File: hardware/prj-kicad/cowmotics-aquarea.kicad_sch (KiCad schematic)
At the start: 0 parts

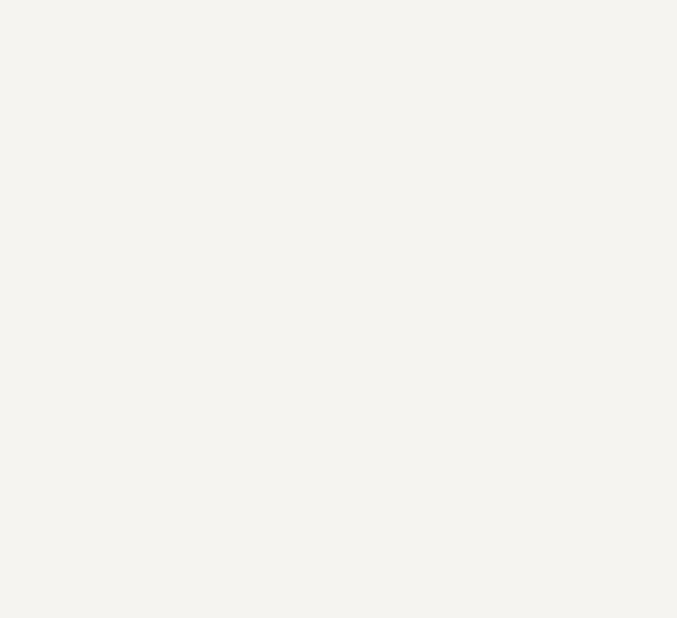
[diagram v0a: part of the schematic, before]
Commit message: = ADD: Insert ESP32 processor and his main components
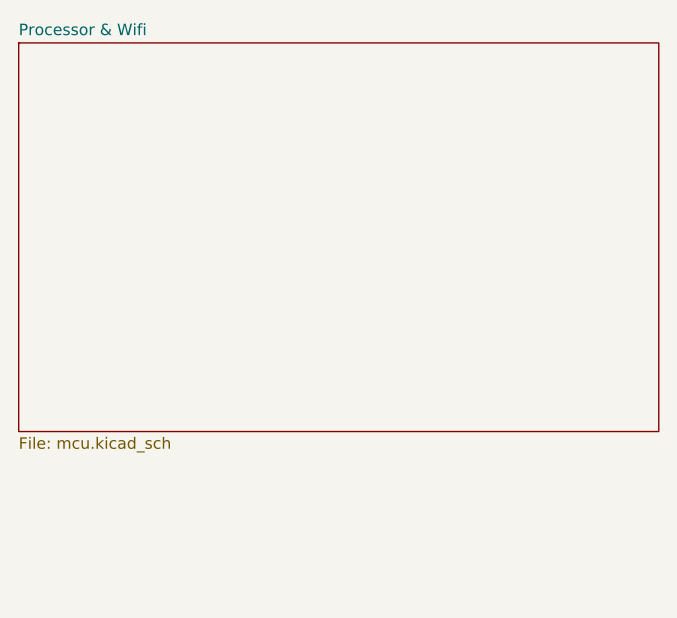
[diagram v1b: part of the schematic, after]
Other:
- added sheet Processor & Wifi (mcu.kicad_sch)
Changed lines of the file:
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@@
+    )
+  )
+  (sheet (at 135.89 33.655) (size 71.12 43.18) (fields_autoplaced)
+    (stroke (width 0.1524) (type solid) (color 0 0 0 0))
+    (fill (color 0 0 0 0.0000))
+    (property "Sheet name" "Processor & Wifi" (id 0) (at 135.89 32.9434 0)
+      (effects (font (size 1.27 1.27)) (justify left bottom))
+    )
+    (property "Sheet file" "mcu.kicad_sch" (id 1) (at 135.89 77.4196 0)
+      (effects (font (size 1.27 1.27)) (justify left top))
     )
   )
@@
     (path "/" (page "1"))
     (path "/38d2e88e-817b-499b-a8dc-6ffe82e53baa" (page "2"))
+    (path "/825065db-dc11-43e9-aa2e-59e6b2cd21f3" (page "3"))
   )
   (symbol_instances
@@
       (reference "#PWR0125") (unit 1) (value "GND") (footprint "")
     )
+    (path "/825065db-dc11-43e9-aa2e-59e6b2cd21f3/aa662617-353d-45f8-8bab-007a7f6b3467"
+      (reference "#PWR0126") (unit 1) (value "GND") (footprint "")
+    )
+    (path "/825065db-dc11-43e9-aa2e-59e6b2cd21f3/f5a690b1-a723-491f-9e65-a4dc1fb25333"
+      (reference "#PWR0127") (unit 1) (value "GND") (footprint "")
+    )
+    (path "/825065db-dc11-43e9-aa2e-59e6b2cd21f3/bb7c498b-0339-4089-b873-6dffa6d6713f"
+      (reference "#PWR0128") (unit 1) (value "GND") (footprint "")
+    )
+    (path "/825065db-dc11-43e9-aa2e-59e6b2cd21f3/367afd26-be8b-422a-ab8f-fbd169ddcc5a"
+      (reference "#PWR0129") (unit 1) (value "GND") (footprint "")
+    )
+    (path "/825065db-dc11-43e9-aa2e-59e6b2cd21f3/98364297-c4ad-454c-b800-3e22ff1db8a3"
+      (reference "#PWR0130") (unit 1) (value "GND") (footprint "")
+    )
+    (path "/825065db-dc11-43e9-aa2e-59e6b2cd21f3/55887181-5e4b-4575-b90e-fe6bb9328e01"
+      (reference "#PWR0131") (unit 1) (value "GND") (footprint "")
+    )
+    (path "/825065db-dc11-43e9-aa2e-59e6b2cd21f3/9cf5069d-7e57-418e-8c23-95dcafcdacf9"
+      (reference "#PWR0132") (unit 1) (value "+3.3V") (footprint "")
+    )
+    (path "/825065db-dc11-43e9-aa2e-59e6b2cd21f3/33c6b2c3-1517-422e-85ee-b8426af14ec5"
+      (reference "#PWR0133") (unit 1) (value "+3.3V") (footprint "")
+    )
+    (path "/825065db-dc11-43e9-aa2e-59e6b2cd21f3/abdb3229-d2e1-49d3-b8de-37b672350f4f"
+      (reference "#PWR0134") (unit 1) (value "+3.3V") (footprint "")
+    )
+    (path "/825065db-dc11-43e9-aa2e-59e6b2cd21f3/a6f2707f-c9c9-4cbb-9ba7-d37e52c8a8a4"
+      (reference "#PWR0135") (unit 1) (value "GND") (footprint "")
+    )
+    (path "/825065db-dc11-43e9-aa2e-59e6b2cd21f3/3ec4ff8a-4c7d-42d9-a1a2-4060e56d921d"
+      (reference "#PWR0136") (unit 1) (value "GND") (footprint "")
+    )
+    (path "/825065db-dc11-43e9-aa2e-59e6b2cd21f3/5bc6b76e-0764-45bf-b282-a3a5393cd86d"
+      (reference "#PWR0137") (unit 1) (value "GND") (footprint "")
+    )
+    (path "/825065db-dc11-43e9-aa2e-59e6b2cd21f3/ac896b10-b56d-48cd-a40f-40aea60ea3de"
+      (reference "#PWR0138") (unit 1) (value "GND") (footprint "")
+    )
+    (path "/825065db-dc11-43e9-aa2e-59e6b2cd21f3/f72bf72c-f5bd-4416-9db8-2d2131c42563"
+      (reference "#PWR0139") (unit 1) (value "+3.3V") (footprint "")
+    )
+    (path "/825065db-dc11-43e9-aa2e-59e6b2cd21f3/2d06930a-3556-4ca4-8e19-ceb5186c902c"
+      (reference "#PWR0140") (unit 1) (value "GND") (footprint "")
+    )
+    (path "/825065db-dc11-43e9-aa2e-59e6b2cd21f3/c1353406-aee2-4fa7-afd8-e1c3846e03ff"
+      (reference "#PWR0141") (unit 1) (value "GND") (footprint "")
+    )
+    (path "/825065db-dc11-43e9-aa2e-59e6b2cd21f3/1a96750d-1856-4066-bb83-1223e7a4075b"
+      (reference "#PWR0142") (unit 1) (value "GND") (footprint "")
+    )
+    (path "/825065db-dc11-43e9-aa2e-59e6b2cd21f3/59a86aaa-3c97-4075-abdb-4a0f75c3444c"
+      (reference "#PWR0143") (unit 1) (value "+VMEM") (footprint "")
+    )
+    (path "/825065db-dc11-43e9-aa2e-59e6b2cd21f3/70b0bb82-e5bb-4e37-8438-bc5be16178cc"
+      (reference "#PWR0144") (unit 1) (value "+VMEM") (footprint "")
+    )
+    (path "/825065db-dc11-43e9-aa2e-59e6b2cd21f3/ab3fca1c-45bb-469f-9f25-aa7e33ef6c3f"
+      (reference "#PWR0145") (unit 1) (value "+VMEM") (footprint "")
+    )
+    (path "/825065db-dc11-43e9-aa2e-59e6b2cd21f3/faf896ff-a31a-44d8-9988-76831a9d862a"
+      (reference "#PWR0146") (unit 1) (value "GND") (footprint "")
+    )
+    (path "/825065db-dc11-43e9-aa2e-59e6b2cd21f3/e7cc7ad7-f806-48cf-ae6e-20dfcc5dcaee"
+      (reference "A1") (unit 1) (value "ANTENNA") (footprint "")
+    )
     (path "/38d2e88e-817b-499b-a8dc-6ffe82e53baa/e4901cdd-b675-43fa-95c2-426e8c824f2f"
       (reference "C1") (unit 1) (value "100nF") (footprint "cowmotics-aquarea:SMD0603")
@@
       (reference "C9") (unit 1) (value "100nF") (footprint "cowmotics-aquarea:SMD0603")
     )
+    (path "/825065db-dc11-43e9-aa2e-59e6b2cd21f3/b412f3cc-d747-49e4-af3e-b05be88e1086"
+      (reference "C11") (unit 1) (value "10pF") (footprint "cowmotics-aquarea:SMD0603")
+    )
+    (path "/825065db-dc11-43e9-aa2e-59e6b2cd21f3/27b131df-df48-47ca-b698-fc59bb8b7b48"
+      (reference "C12") (unit 1) (value "10pF") (footprint "cowmotics-aquarea:SMD0603")
+    )
+    (path "/825065db-dc11-43e9-aa2e-59e6b2cd21f3/dc627a33-8631-4bf7-9cfa-e7d61c1c50ec"
+      (reference "C13") (unit 1) (value "10nF") (footprint "cowmotics-aquarea:SMD0603")
+    )
+    (path "/825065db-dc11-43e9-aa2e-59e6b2cd21f3/055bd41d-4d87-4a49-9e0d-ec28a81d5e69"
+      (reference "C14") (unit 1) (value "10nF") (footprint "cowmotics-aquarea:SMD0603")
+    )
+    (path "/825065db-dc11-43e9-aa2e-59e6b2cd21f3/1da82e5d-dfed-41b2-ba5e-3a1d68571e18"
+      (reference "C15") (unit 1) (value "3,3nF") (footprint "cowmotics-aquarea:SMD0603")
+    )
+    (path "/825065db-dc11-43e9-aa2e-59e6b2cd21f3/2e5dae1f-76cb-4c37-85a0-30b2c21af63f"
+      (reference "C16") (unit 1) (value "C") (footprint "cowmotics-aquarea:SMD0603")
+    )
+    (path "/825065db-dc11-43e9-aa2e-59e6b2cd21f3/cc4d6061-2845-4d3f-a4f9-82eeb84d6d9f"
+      (reference "C17") (unit 1) (value "C") (footprint "cowmotics-aquarea:SMD0603")
+    )
+    (path "/825065db-dc11-43e9-aa2e-59e6b2cd21f3/aaea601f-301e-4b17-bbc4-978a8026e72b"
+      (reference "C18") (unit 1) (value "1uF") (footprint "cowmotics-aquarea:SMD0603")
+    )
+    (path "/825065db-dc11-43e9-aa2e-59e6b2cd21f3/8ec30f0d-54f3-4133-ad28-83d66580ed3b"
+      (reference "C19") (unit 1) (value "100nF") (footprint "cowmotics-aquarea:SMD0603")
+    )
+    (path "/825065db-dc11-43e9-aa2e-59e6b2cd21f3/9d2bfb75-3655-468a-99b3-1689c86cc127"
+      (reference "C20") (unit 1) (value "100nF") (footprint "cowmotics-aquarea:SMD0603")
+    )
     (path "/38d2e88e-817b-499b-a8dc-6ffe82e53baa/18a9dea8-caa6-40a3-962a-7699d9146e17"
       (reference "J1") (unit 1) (value "CONN_RJ45") (footprint "cowmotics-aquarea:CONN_615008185121")
@@
       (reference "L1") (unit 1) (value "FB100") (footprint "cowmotics-aquarea:SMD0603")
     )
+    (path "/825065db-dc11-43e9-aa2e-59e6b2cd21f3/36f39277-833d-4032-80bf-37be5c675044"
+      (reference "L2") (unit 1) (value "FB100") (footprint "cowmotics-aquarea:SMD0603")
+    )
+    (path "/825065db-dc11-43e9-aa2e-59e6b2cd21f3/0d087c84-db65-4f93-8a04-a5da574852b7"
+      (reference "L3") (unit 1) (value "INDUCTOR") (footprint "cowmotics-aquarea:SMD0603")
+    )
     (path "/38d2e88e-817b-499b-a8dc-6ffe82e53baa/bea8a93b-5d86-4516-aa08-d642cf48f2e6"
       (reference "Q1") (unit 1) (value "BC846") (footprint "cowmotics-aquarea:SOT23-3")
@@
       (reference "R12") (unit 1) (value "10k") (footprint "cowmotics-aquarea:SMD0603")
     )
+    (path "/825065db-dc11-43e9-aa2e-59e6b2cd21f3/0df40f43-d59d-4bf1-b2e8-22aead9235c5"
+      (reference "R15") (unit 1) (value "10k") (footprint "cowmotics-aquarea:SMD0603")
+    )
+    (path "/825065db-dc11-43e9-aa2e-59e6b2cd21f3/ac2da823-4699-45dd-9813-e8de59e5d43b"
+      (reference "R16") (unit 1) (value "20k") (footprint "cowmotics-aquarea:SMD0603")
+    )
     (path "/38d2e88e-817b-499b-a8dc-6ffe82e53baa/a56deef6-ff70-4f97-bfaa-cc479299031a"
       (reference "T1") (unit 1) (value "TRANSFORMER_1_1") (footprint "cowmotics-aquarea:TR_W749013011")
@@
       (reference "U1") (unit 1) (value "KSZ8091RN") (footprint "cowmotics-aquarea:QFN24")
     )
+    (path "/825065db-dc11-43e9-aa2e-59e6b2cd21f3/53eb5fc0-41cc-43ad-8003-3a7163adca82"
+      (reference "U2") (unit 1) (value "ESP32") (footprint "cowmotics-aquarea:QFN48-04")
+    )
+    (path "/825065db-dc11-43e9-aa2e-59e6b2cd21f3/6ead67cb-c858-432f-8293-babe98d42987"
+      (reference "U2") (unit 2) (value "ESP32") (footprint "cowmotics-aquarea:QFN48-04")
+    )
+    (path "/825065db-dc11-43e9-aa2e-59e6b2cd21f3/f5db3b34-82eb-4087-85c1-08c4586de2aa"
+      (reference "U3") (unit 1) (value "SST25VF016") (footprint "cowmotics-aquarea:SOIC-8")
+    )
     (path "/38d2e88e-817b-499b-a8dc-6ffe82e53baa/bdfc4715-c6ee-47ec-8978-077838963a54"
       (reference "X1") (unit 1) (value "50MHz") (footprint "cowmotics-aquarea:Q_SMD5x3")
     )
-  )
+    (path "/825065db-dc11-43e9-aa2e-59e6b2cd21f3/bdbb5037-e302-4f21-aecd-679af5c21a62"
+      (reference "X2") (unit 1) (value "40MHz") (footprint "cowmotics-aquarea:Q_3.2x2.5")
+    )
+  )

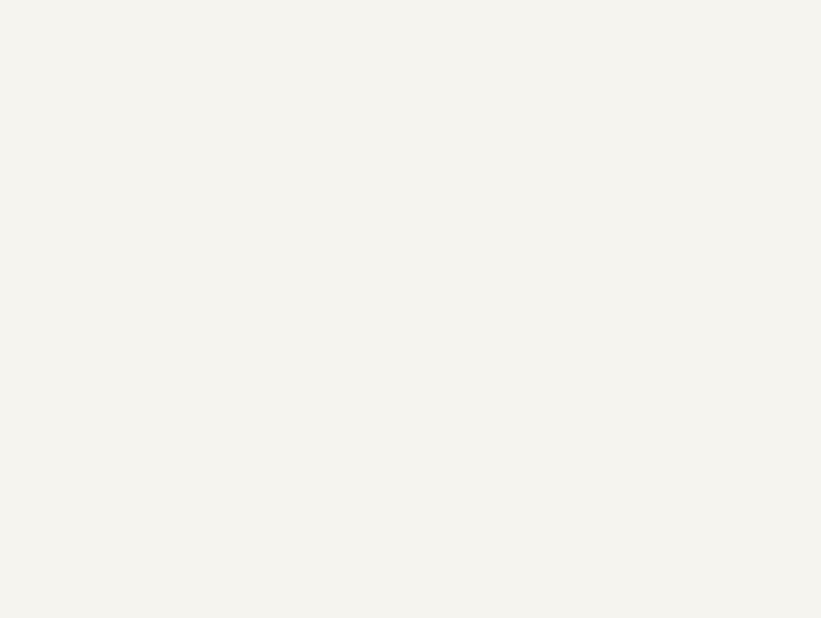
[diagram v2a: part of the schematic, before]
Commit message: = ADD: Insert Aquarea serial interface and power supply
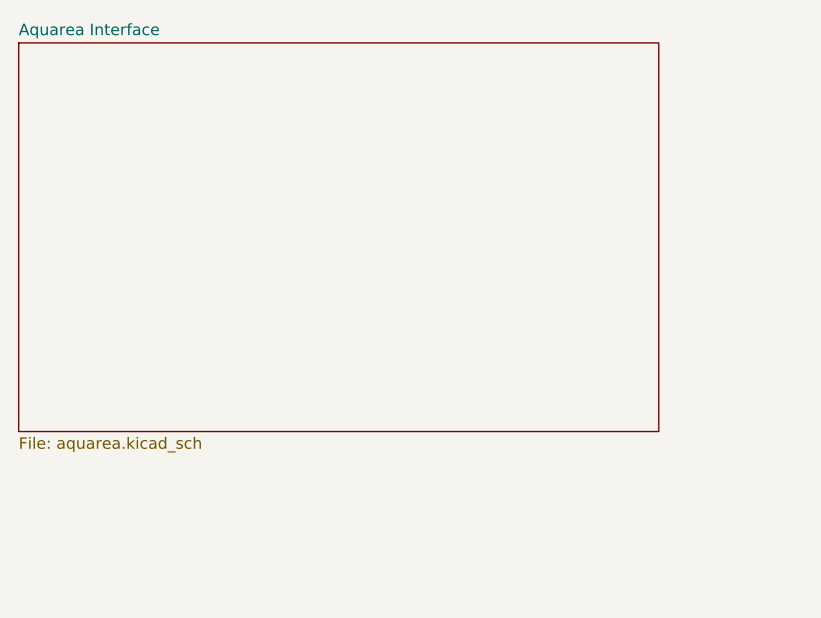
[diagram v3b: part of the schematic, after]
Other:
- added sheet Aquarea Interface (aquarea.kicad_sch)
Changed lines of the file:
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@@
+    )
+  )
+  (sheet (at 33.655 33.655) (size 71.12 43.18) (fields_autoplaced)
+    (stroke (width 0.1524) (type solid) (color 0 0 0 0))
+    (fill (color 0 0 0 0.0000))
+    (property "Sheet name" "Aquarea Interface" (id 0) (at 33.655 32.9434 0)
+      (effects (font (size 1.27 1.27)) (justify left bottom))
+    )
+    (property "Sheet file" "aquarea.kicad_sch" (id 1) (at 33.655 77.4196 0)
+      (effects (font (size 1.27 1.27)) (justify left top))
     )
   )
@@
     (path "/38d2e88e-817b-499b-a8dc-6ffe82e53baa" (page "2"))
     (path "/825065db-dc11-43e9-aa2e-59e6b2cd21f3" (page "3"))
+    (path "/98155800-78e7-48e2-b416-a5948d22b132" (page "4"))
   )
   (symbol_instances
@@
       (reference "#PWR0154") (unit 1) (value "GND") (footprint "")
     )
+    (path "/98155800-78e7-48e2-b416-a5948d22b132/a24579c0-8f16-4c68-b896-1ec34d92a6c4"
+      (reference "#PWR0155") (unit 1) (value "+5V") (footprint "")
+    )
+    (path "/98155800-78e7-48e2-b416-a5948d22b132/df4a707f-c422-45b9-846e-5f8beda1b995"
+      (reference "#PWR0156") (unit 1) (value "GND") (footprint "")
+    )
+    (path "/98155800-78e7-48e2-b416-a5948d22b132/8941ba23-15e2-4939-ba0d-2ca7f1f5ac1b"
+      (reference "#PWR0157") (unit 1) (value "+3.3V") (footprint "")
+    )
+    (path "/98155800-78e7-48e2-b416-a5948d22b132/f8b6bb9f-ad03-4bcb-9251-2a066978a098"
+      (reference "#PWR0158") (unit 1) (value "+5V") (footprint "")
+    )
+    (path "/98155800-78e7-48e2-b416-a5948d22b132/deb3c8d4-cd4a-4c3f-9749-bd9ef6b7b0d7"
+      (reference "#PWR0159") (unit 1) (value "GND") (footprint "")
+    )
+    (path "/98155800-78e7-48e2-b416-a5948d22b132/2523fb7d-bdf6-476e-87d5-a6e44e66f2d6"
+      (reference "#PWR0160") (unit 1) (value "+12V") (footprint "")
+    )
+    (path "/98155800-78e7-48e2-b416-a5948d22b132/ae02e6ad-b22a-4981-9b68-ea9b5483cbf0"
+      (reference "#PWR0161") (unit 1) (value "+5V") (footprint "")
+    )
+    (path "/98155800-78e7-48e2-b416-a5948d22b132/cc9ecc58-049e-4be1-b641-c31882f37ca7"
+      (reference "#PWR0162") (unit 1) (value "+3.3V") (footprint "")
+    )
+    (path "/98155800-78e7-48e2-b416-a5948d22b132/4e51c7be-5689-4060-9944-a768ee0964e6"
+      (reference "#PWR0163") (unit 1) (value "GND") (footprint "")
+    )
+    (path "/98155800-78e7-48e2-b416-a5948d22b132/76d96292-67d7-4661-baf1-dfdd20b23b48"
+      (reference "#PWR0164") (unit 1) (value "GND") (footprint "")
+    )
+    (path "/98155800-78e7-48e2-b416-a5948d22b132/8c35d187-d2af-4c4c-a5db-5041491ae221"
+      (reference "#PWR0165") (unit 1) (value "+3.3V") (footprint "")
+    )
+    (path "/98155800-78e7-48e2-b416-a5948d22b132/960e3980-6992-4f2f-be18-9d55b25deb4f"
+      (reference "#PWR0166") (unit 1) (value "+5V") (footprint "")
+    )
+    (path "/98155800-78e7-48e2-b416-a5948d22b132/646eb608-8655-4892-b3d9-d0c69b132ad5"
+      (reference "#PWR0167") (unit 1) (value "GND") (footprint "")
+    )
+    (path "/98155800-78e7-48e2-b416-a5948d22b132/dd76ffd3-cf84-4264-9b48-46e38b2e06ed"
+      (reference "#PWR0168") (unit 1) (value "GND") (footprint "")
+    )
+    (path "/98155800-78e7-48e2-b416-a5948d22b132/070569f3-8118-41a9-ae0d-9ac889645e9d"
+      (reference "#PWR0169") (unit 1) (value "GND") (footprint "")
+    )
+    (path "/98155800-78e7-48e2-b416-a5948d22b132/105c56d1-30e6-4a56-976f-42759cb1f7f2"
+      (reference "#PWR0170") (unit 1) (value "+3.3V") (footprint "")
+    )
+    (path "/98155800-78e7-48e2-b416-a5948d22b132/8152e6f5-b60f-4c0c-ac89-7de02362ab60"
+      (reference "#PWR0171") (unit 1) (value "GND") (footprint "")
+    )
+    (path "/98155800-78e7-48e2-b416-a5948d22b132/05b16ca9-6086-4d32-aa87-2738c8656874"
+      (reference "#PWR0172") (unit 1) (value "+12V") (footprint "")
+    )
+    (path "/98155800-78e7-48e2-b416-a5948d22b132/6da368c0-01b4-4b20-8f83-3377f60df388"
+      (reference "#PWR0173") (unit 1) (value "GND") (footprint "")
+    )
+    (path "/98155800-78e7-48e2-b416-a5948d22b132/1302e146-4d18-4a35-b511-025dc46a5910"
+      (reference "#PWR0174") (unit 1) (value "+5V") (footprint "")
+    )
+    (path "/98155800-78e7-48e2-b416-a5948d22b132/110987fe-4f33-4568-96f4-a15ba51a26fb"
+      (reference "#PWR0175") (unit 1) (value "GND") (footprint "")
+    )
+    (path "/98155800-78e7-48e2-b416-a5948d22b132/12fa97ca-9c7c-4df1-bac7-aa03d210c139"
+      (reference "#PWR0176") (unit 1) (value "GND") (footprint "")
+    )
+    (path "/98155800-78e7-48e2-b416-a5948d22b132/035aefe0-7417-4380-8cad-ff04e2942bb6"
+      (reference "#PWR0177") (unit 1) (value "GND") (footprint "")
+    )
+    (path "/98155800-78e7-48e2-b416-a5948d22b132/2397e841-1be1-415f-a1b9-7ff8d54aff04"
+      (reference "#PWR0178") (unit 1) (value "+3.3V") (footprint "")
+    )
     (path "/825065db-dc11-43e9-aa2e-59e6b2cd21f3/e7cc7ad7-f806-48cf-ae6e-20dfcc5dcaee"
       (reference "A1") (unit 1) (value "ANTENNA") (footprint "cowmotics-aquarea:CONN_SMA_RA")
@@
       (reference "C23") (unit 1) (value "1uF") (footprint "cowmotics-aquarea:SMD0603")
     )
+    (path "/98155800-78e7-48e2-b416-a5948d22b132/53279ea3-2f0b-40ec-b25e-0a09cafac841"
+      (reference "C25") (unit 1) (value "10uF") (footprint "cowmotics-aquarea:SMD1210")
+    )
+    (path "/98155800-78e7-48e2-b416-a5948d22b132/113db992-658b-4f23-8b16-4522e5d594a2"
+      (reference "C26") (unit 1) (value "100nF") (footprint "cowmotics-aquarea:SMD0603")
+    )
+    (path "/98155800-78e7-48e2-b416-a5948d22b132/8d3a9eec-e9a7-4f7a-a913-1c4b83c46ec3"
+      (reference "C27") (unit 1) (value "100nF") (footprint "cowmotics-aquarea:SMD0603")
+    )
+    (path "/98155800-78e7-48e2-b416-a5948d22b132/7844fa1c-c2e9-46d4-aee9-55128915096f"
+      (reference "C28") (unit 1) (value "10uF") (footprint "cowmotics-aquarea:SMD1210")
+    )
+    (path "/98155800-78e7-48e2-b416-a5948d22b132/e82ebb99-a6b9-48fa-9aa1-331985f42c93"
+      (reference "C29") (unit 1) (value "470pF") (footprint "cowmotics-aquarea:SMD0603")
+    )
+    (path "/98155800-78e7-48e2-b416-a5948d22b132/b3b5d4a8-a7a4-4bdd-91c8-1d396734d302"
+      (reference "C30") (unit 1) (value "4,7uF") (footprint "cowmotics-aquarea:SMD0603")
+    )
+    (path "/98155800-78e7-48e2-b416-a5948d22b132/feda6d61-2233-4f26-b0c5-c1eee19352ad"
+      (reference "C31") (unit 1) (value "4,7uF") (footprint "cowmotics-aquarea:SMD0603")
+    )
     (path "/38d2e88e-817b-499b-a8dc-6ffe82e53baa/18a9dea8-caa6-40a3-962a-7699d9146e17"
       (reference "J1") (unit 1) (value "CONN_RJ45") (footprint "cowmotics-aquarea:CONN_615008185121")
     )
+    (path "/98155800-78e7-48e2-b416-a5948d22b132/91125ed1-04ac-414b-89bd-9ef46367e239"
+      (reference "J2") (unit 1) (value "CONN_5") (footprint "cowmotics-aquarea:CONN_691243310005")
+    )
     (path "/38d2e88e-817b-499b-a8dc-6ffe82e53baa/ec075aee-9a67-4dd0-9403-ff58215d0638"
       (reference "L1") (unit 1) (value "FB100") (footprint "cowmotics-aquarea:SMD0603")
@@
       (reference "L3") (unit 1) (value "INDUCTOR") (footprint "cowmotics-aquarea:SMD0603")
     )
+    (path "/98155800-78e7-48e2-b416-a5948d22b132/84c6da4f-5623-4a9c-a50d-ae757f720ada"
+      (reference "L4") (unit 1) (value "2,2uH") (footprint "cowmotics-aquarea:I_CDRH2D14")
+    )
     (path "/38d2e88e-817b-499b-a8dc-6ffe82e53baa/bea8a93b-5d86-4516-aa08-d642cf48f2e6"
       (reference "Q1") (unit 1) (value "BC846") (footprint "cowmotics-aquarea:SOT23-3")
@@
       (reference "U3") (unit 1) (value "SST25VF016") (footprint "cowmotics-aquarea:SOIC-8")
     )
+    (path "/98155800-78e7-48e2-b416-a5948d22b132/5460fda9-d078-489b-9094-c02aef678b0d"
+      (reference "U4") (unit 1) (value "SN74LVC1T45") (footprint "cowmotics-aquarea:SOT23-6")
+    )
+    (path "/98155800-78e7-48e2-b416-a5948d22b132/2d49add9-f626-4c40-beb6-abf539c8ce3f"
+      (reference "U5") (unit 1) (value "SN74LVC1T45") (footprint "cowmotics-aquarea:SOT23-6")
+    )
+    (path "/98155800-78e7-48e2-b416-a5948d22b132/f9a96519-3311-4449-9395-320ce48a3d34"
+      (reference "U6") (unit 1) (value "LM3671") (footprint "cowmotics-aquarea:SOT23-5")
+    )
     (path "/38d2e88e-817b-499b-a8dc-6ffe82e53baa/bdfc4715-c6ee-47ec-8978-077838963a54"
